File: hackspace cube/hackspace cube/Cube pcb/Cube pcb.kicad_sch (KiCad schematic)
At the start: 57 parts, among them J1 Conn_01x09 ( conector 1), J2 Conn_01x09 ( conector 2), J3 Conn_01x02 ( exstra ground co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, J4 Conn_01x14 ( Spare Ports ), Q1 BSS138, Q10 BSS138, Q11 BSS138, Q12 BSS138, Q13 BSS138, Q14 BSS138, Q15 BSS138, Q16 BSS138, Q2 BSS138, Q3 BSS138, Q4 BSS138, Q5 BSS138, Q6 BSS138, Q7 BSS138, Q8 BSS138, Q9 BSS138

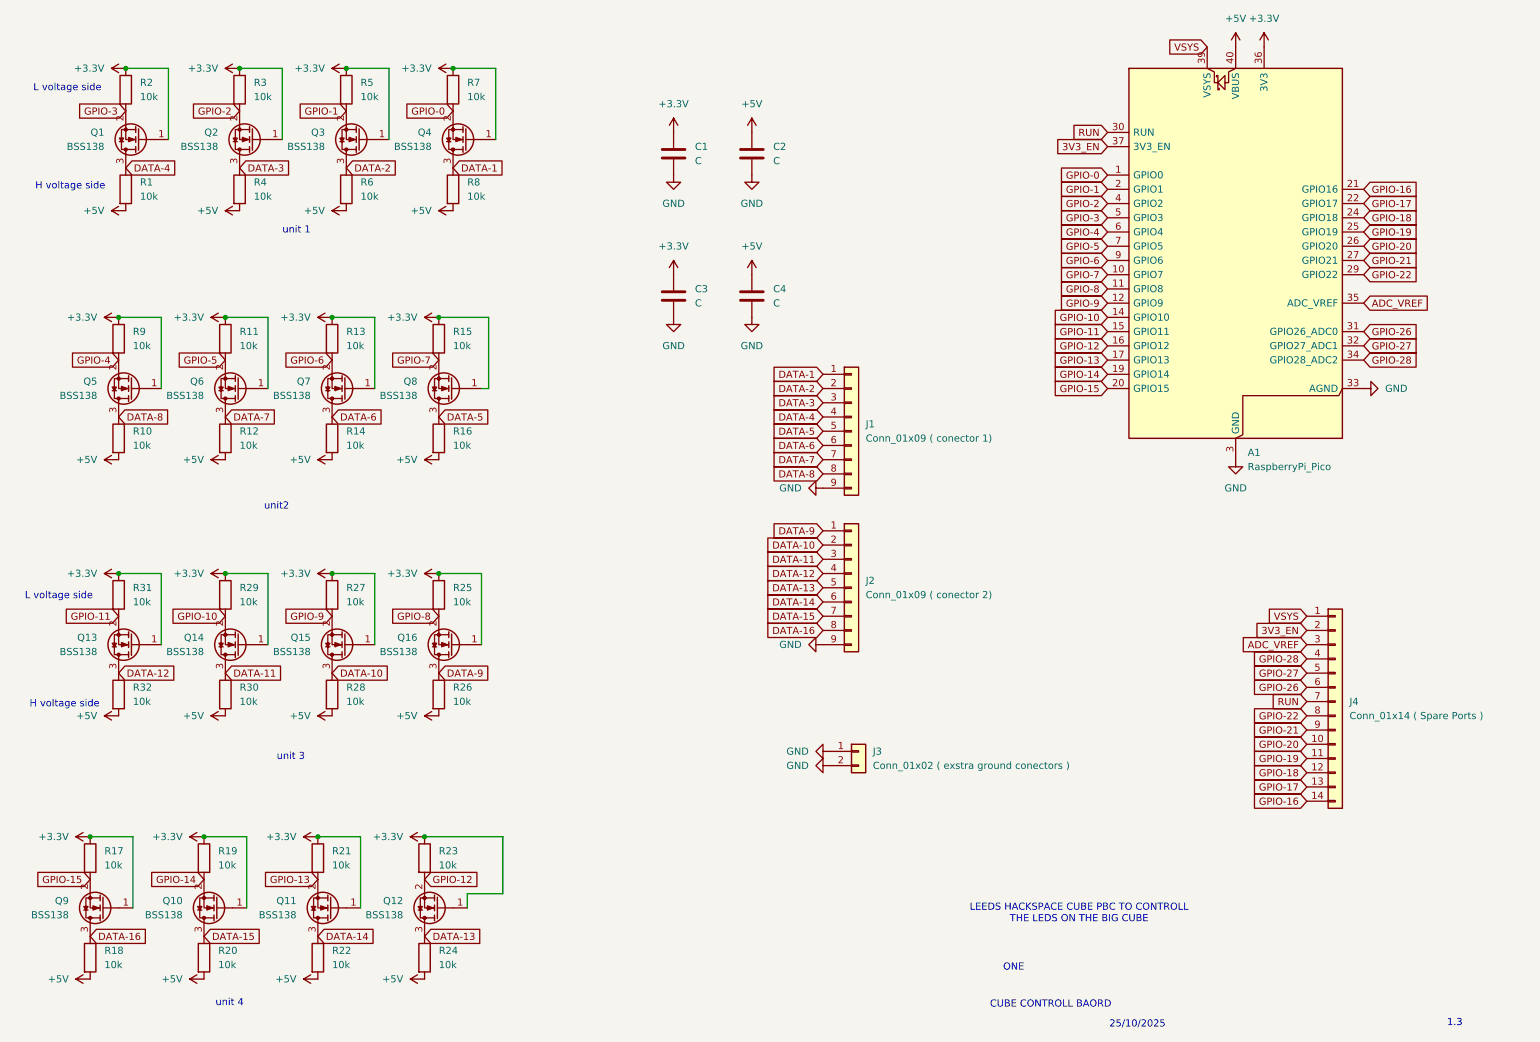
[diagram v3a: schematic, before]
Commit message: rev 1.4
added new smooth caps and updated pcb
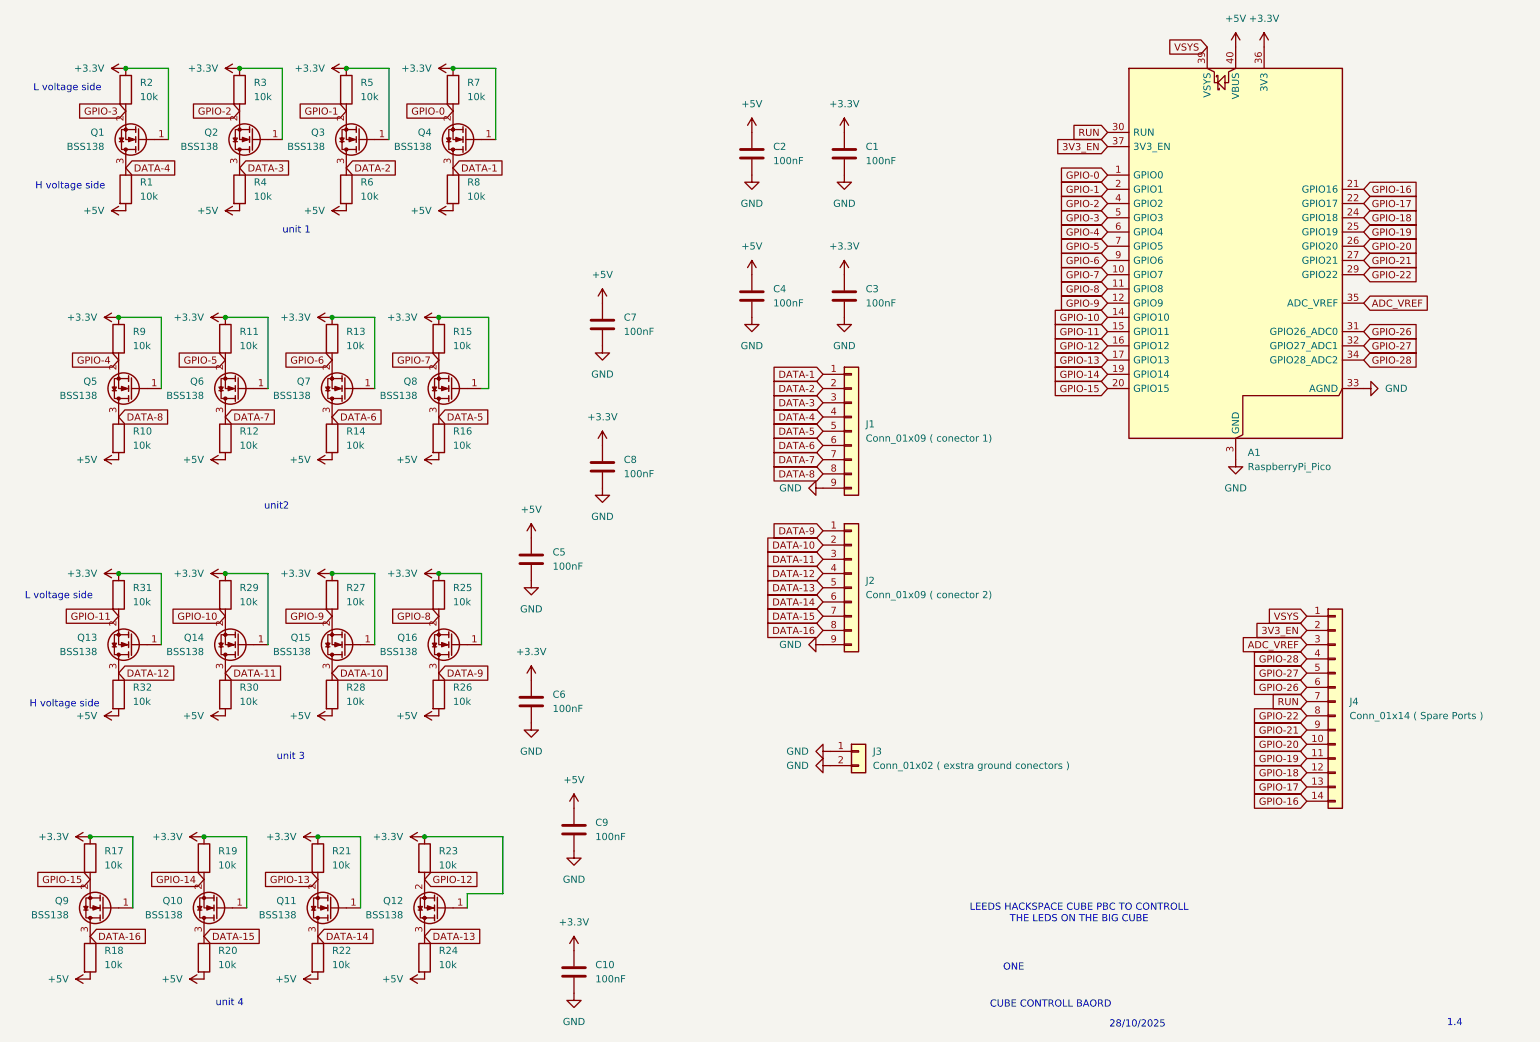
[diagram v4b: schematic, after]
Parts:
- added C10, C5, C6, C7, C8, C9: 100nF, Capacitor_SMD:C_0805_2012Metric, symbol Device:C
- C1, C2, C3, C4: value C -> 100nF
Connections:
- net +3.3V: now also C10.1, C6.1, C8.1
- net +5V: now also C5.1, C7.1, C9.1
- net GND: now also C10.2, C5.2, C6.2, C7.2, C8.2, C9.2
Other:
- note added: "1.4"
- note added: "28/10/2025"
- note removed: "1.3"
- note removed: "25/10/2025"
- moved on the sheet: C1, C3
